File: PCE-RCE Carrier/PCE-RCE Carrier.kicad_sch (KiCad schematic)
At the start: 2 parts, among them J5 DF40C-34DP-0.4V_58_, J7 DF40C-34DP-0.4V_58_

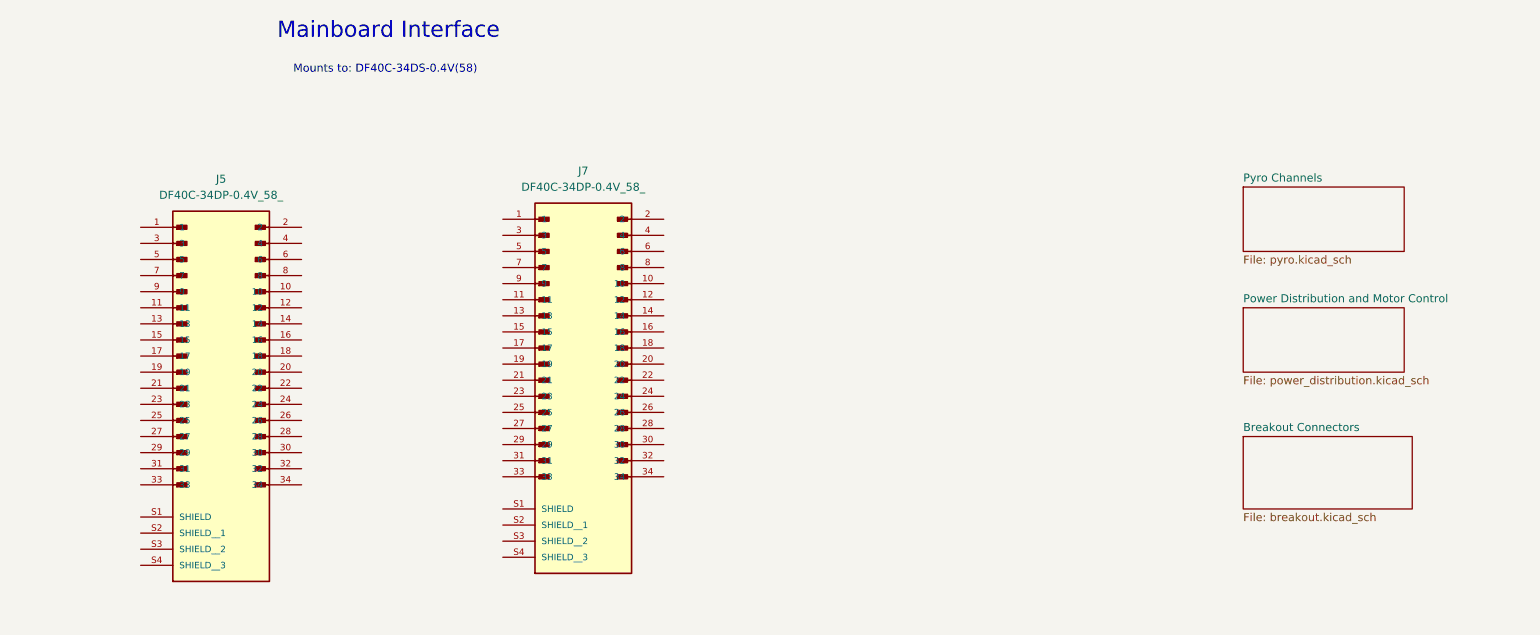
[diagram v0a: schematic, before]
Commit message: H-Bridge wiring + motor ports, cleaned up carrier schematics, added MISO source terminating resistors on carriers
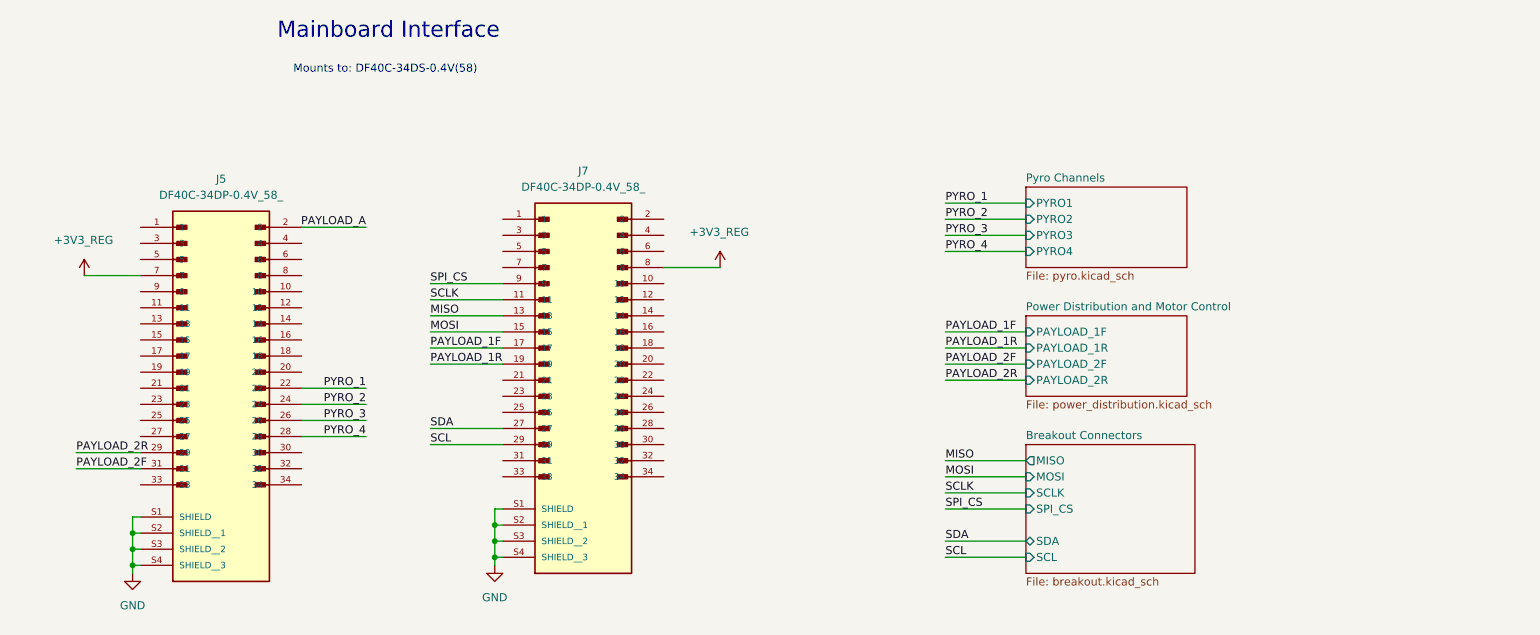
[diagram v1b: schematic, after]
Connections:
- net SCLK: now reaches J7.11
- net MISO: now reaches J7.13
- net MOSI: now reaches J7.15
- net PAYLOAD_1F: now reaches J7.17
- net PAYLOAD_1R: now reaches J7.19
- net SDA: now reaches J7.27
- net SCL: now reaches J7.29
- net +3V3_REG: now reaches J7.8
- net +3V3_REG: now also J5.7
- net SPI_CS: now reaches J7.9
- net GND: now reaches J7.S1 (SHIELD)
- net GND: now also J5.S1 (SHIELD), J5.S2 (SHIELD__1), J5.S3 (SHIELD__2), J5.S4 (SHIELD__3), J7.S2 (SHIELD__1), J7.S3 (SHIELD__2), J7.S4 (SHIELD__3)
- net PAYLOAD_A: now reaches J5.2
- net PYRO_1: now reaches J5.22
- net PYRO_2: now reaches J5.24
- net PYRO_3: now reaches J5.26
- net PYRO_4: now reaches J5.28
- net PAYLOAD_2R: now reaches J5.29
- net PAYLOAD_2F: now reaches J5.31
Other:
- sheet Breakout Connectors ports: added MISO, MOSI, SCL, SCLK, SDA, SPI_CS; removed none
- sheet Power Distribution and Motor Control ports: added PAYLOAD_1F, PAYLOAD_1R, PAYLOAD_2F, PAYLOAD_2R; removed none
- sheet Pyro Channels ports: added PYRO1, PYRO2, PYRO3, PYRO4; removed none

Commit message: carrier board comments
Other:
- sheet Pyro Channels ports: added PYRO_1, PYRO_2, PYRO_3, PYRO_4; removed PYRO1, PYRO2, PYRO3, PYRO4
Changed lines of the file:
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@@
 			)
 		)
-		(pin "PYRO1" input
+		(pin "PYRO_1" input
 			(at 187.96 91.44 180)
 			(effects
@@
 			)
 		)
-		(pin "PYRO2" input
+		(pin "PYRO_2" input
 			(at 187.96 93.98 180)
 			(effects
@@
 			)
 		)
-		(pin "PYRO3" input
+		(pin "PYRO_3" input
 			(at 187.96 96.52 180)
 			(effects
@@
 			)
 		)
-		(pin "PYRO4" input
+		(pin "PYRO_4" input
 			(at 187.96 99.06 180)
 			(effects

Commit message: footprint libraries and initial board setup
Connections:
- net +3V3_REG: now also J7.12; no longer J7.8
- net GND: now also J5.1, J5.11, J5.25, J5.9, J7.1, J7.2, J7.32, J7.34, J7.7
- net PAYLOAD_1F: now also J5.14; no longer J7.17
- net PAYLOAD_1R: now also J5.16; no longer J7.19
- net PAYLOAD_2F: now also J7.23; no longer J5.31
- net PAYLOAD_2R: now also J7.21; no longer J5.29
- net PYRO_1: now also J7.33; no longer J5.22
- net PYRO_2: now also J7.31; no longer J5.24
- net PYRO_3: now also J7.29; no longer J5.26
- net PYRO_4: now also J7.27; no longer J5.28
- net SCL: now also J5.10; no longer J7.29
- net SDA: now also J5.8; no longer J7.27
- net PYRO_5: now reaches J7.25
- no-connect marks 0 -> 21

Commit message: updated pyro circuit to be like easymini, lowk will prob make it a separate carrier
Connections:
- net PAYLOAD_A: now also J5.28; no longer J5.2
- no-connect marks 21 -> 22
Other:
- sheet Breakout Connectors ports: added PADYLOAD_A; removed none
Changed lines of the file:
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@@
+	)
+	(no_connect
+		(at 73.66 95.25)
 	)
 	(no_connect
@@
 	(wire
 		(pts
+			(xy 73.66 128.27) (xy 85.09 128.27)
+		)
+		(stroke
+			(width 0)
+			(type default)
+		)
+	)
+	(wire
+		(pts
 			(xy 93.98 132.08) (xy 105.41 132.08)
 		)
@@
 	(wire
 		(pts
-			(xy 73.66 95.25) (xy 85.09 95.25)
-		)
-		(stroke
-			(width 0)
-			(type default)
-		)
-	)
-	(wire
-		(pts
 			(xy 105.41 93.98) (xy 91.44 93.98)
 		)
@@
 		)
 	)
-	(label "PAYLOAD_A"
-		(at 85.09 95.25 180)
-		(effects
-			(font
-				(size 1.27 1.27)
-			)
-			(justify right bottom)
+	(wire
+		(pts
+			(xy 175.26 152.4) (xy 187.96 152.4)
+		)
+		(stroke
+			(width 0)
+			(type default)
 		)
 	)
@@
 		)
 	)
+	(label "PAYLOAD_A"
+		(at 175.26 152.4 0)
+		(effects
+			(font
+				(size 1.27 1.27)
+			)
+			(justify left bottom)
+		)
+	)
 	(label "MOSI"
 		(at 93.98 111.76 0)
@@
 			)
 			(justify left bottom)
+		)
+	)
+	(label "PAYLOAD_A"
+		(at 85.09 128.27 180)
+		(effects
+			(font
+				(size 1.27 1.27)
+			)
+			(justify right bottom)
 		)
 	)
@@
 	(sheet
 		(at 187.96 129.54)
-		(size 26.67 20.32)
+		(size 26.67 25.4)
 		(exclude_from_sim no)
 		(in_bom yes)
@@
 		)
 		(property "Sheetfile" "breakout.kicad_sch"
-			(at 187.96 150.4446 0)
+			(at 187.96 155.5246 0)
 			(show_name no)
 			(do_not_autoplace no)
@@
 			(effects
 				(font
+					(size 1.27 1.27)
+				)
+				(justify left)
+			)
+		)
+		(pin "PADYLOAD_A" output
+			(at 187.96 152.4 180)
+			(effects
+				(font
